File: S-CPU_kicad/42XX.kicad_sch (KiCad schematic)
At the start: 161 parts, among them U34 OR_2, U35 OR_2, U36 OR_2, U37 OR_2, U6 MUX

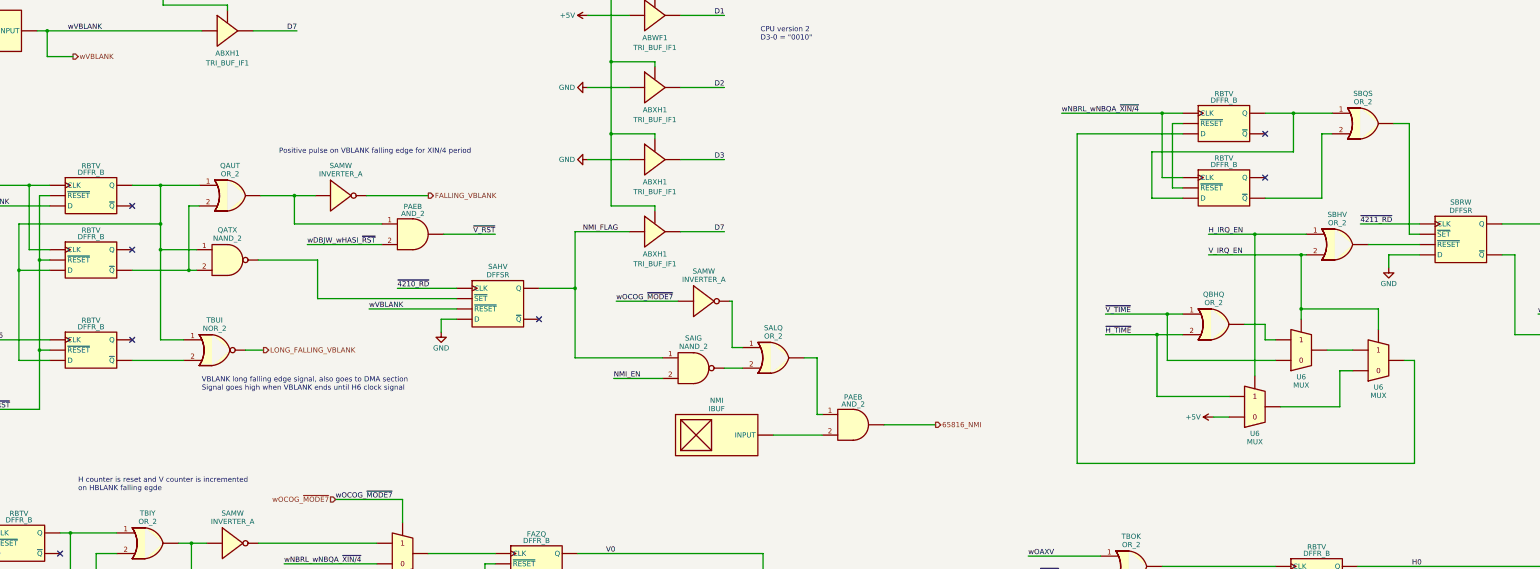
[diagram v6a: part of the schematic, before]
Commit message: DMA section update. Found errors between some MUX and MUXI gates.
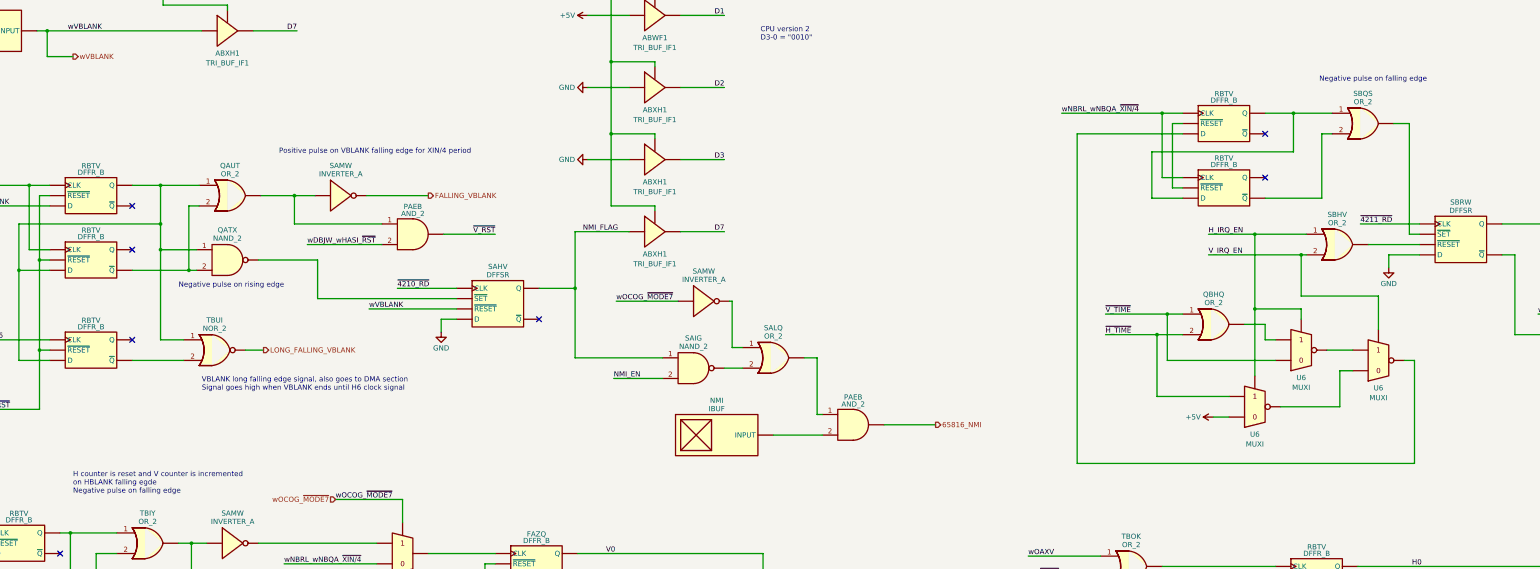
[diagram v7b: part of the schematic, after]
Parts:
- U6: value MUX -> MUXI; symbol Ricoh_Cells:MUX -> Ricoh_Cells:MUXI
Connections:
- net H_IRQ_EN: now also U6.1
- net V_IRQ_EN: no longer U6.1
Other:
- note added: "H counter is reset and V counter is incremented on HBLANK falling egde Negative pulse on falling edge"
- note added: "Negative pulse on falling edge"
- note added: "Negative pulse on rising edge"
- note removed: "H counter is reset and V counter is incremented on HBLANK falling egde"
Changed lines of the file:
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@@
   (junction (at 120.015 297.18) (diameter 0) (color 0 0 0 0)
   )
+  (junction (at 602.615 163.83) (diameter 0) (color 0 0 0 0)
+  )
   (junction (at 173.355 403.86) (diameter 0) (color 0 0 0 0)
   )
@@
   (junction (at 122.555 377.19) (diameter 0) (color 0 0 0 0)
   )
-  (junction (at 614.045 163.83) (diameter 0) (color 0 0 0 0)
-  )
   (junction (at 173.355 288.29) (diameter 0) (color 0 0 0 0)
   )
@@
     (stroke (width 0) (type default))
   )
-  (wire (pts (xy 633.095 163.83) (xy 614.045 163.83))
+  (wire (pts (xy 633.095 160.655) (xy 614.045 160.655))
     (stroke (width 0) (type default))
   )
@@
     (stroke (width 0) (type default))
   )
-  (wire (pts (xy 633.095 168.91) (xy 633.095 163.83))
+  (wire (pts (xy 633.095 168.91) (xy 633.095 160.655))
     (stroke (width 0) (type default))
   )
@@
     (stroke (width 0) (type default))
   )
-  (wire (pts (xy 614.045 150.495) (xy 614.045 163.83))
+  (wire (pts (xy 614.045 150.495) (xy 614.045 160.655))
     (stroke (width 0) (type default))
   )
@@
     (stroke (width 0) (type default))
   )
-  (wire (pts (xy 602.615 145.415) (xy 602.615 180.34))
+  (wire (pts (xy 602.615 145.415) (xy 602.615 163.83))
     (stroke (width 0) (type default))
   )
@@
     (stroke (width 0) (type default))
   )
+  (wire (pts (xy 602.615 163.83) (xy 602.615 180.34))
+    (stroke (width 0) (type default))
+  )
   (wire (pts (xy 132.715 236.22) (xy 147.32 236.22))
     (stroke (width 0) (type default))
@@
     (stroke (width 0) (type dash))
   )
+  (wire (pts (xy 614.045 163.83) (xy 602.615 163.83))
+    (stroke (width 0) (type default))
+  )
   (wire (pts (xy 147.32 283.21) (xy 127.635 283.21))
     (stroke (width 0) (type default))
@@
     (stroke (width 0) (type default))
   )
+  (wire (pts (xy 614.045 166.37) (xy 614.045 163.83))
+    (stroke (width 0) (type default))
+  )
   (wire (pts (xy 341.63 149.225) (xy 332.74 149.225))
     (stroke (width 0) (type default))
@@
     (stroke (width 0) (type default))
   )
-  (wire (pts (xy 614.045 163.83) (xy 614.045 166.37))
-    (stroke (width 0) (type default))
-  )
   (wire (pts (xy 147.32 346.71) (xy 120.015 346.71))
     (stroke (width 0) (type default))
@@
     (effects (font (size 5 5) (thickness 1) bold) (justify left bottom))
   )
+  (text "Negative pulse on rising edge" (at 337.185 158.75 0)
+    (effects (font (size 1.27 1.27)) (justify left bottom))
+  )
   (text "Positive pulse on VBLANK falling edge for XIN/4 period"
     (at 361.95 125.73 0)
@@
     (effects (font (size 2 2)) (justify left bottom))
   )
-  (text "H counter is reset and V counter is incremented\non HBLANK falling egde"
-    (at 312.42 208.915 0)
+  (text "H counter is reset and V counter is incremented\non HBLANK falling egde\nNegative pulse on falling edge"
+    (at 311.15 209.55 0)
     (effects (font (size 1.27 1.27)) (justify left bottom))
   )
@@
     (effects (font (size 5 5) (thickness 1) bold) (justify left bottom))
   )
+  (text "Negative pulse on falling edge" (at 618.49 107.95 0)
+    (effects (font (size 1.27 1.27)) (justify left bottom))
+  )
   (text "4210 READ" (at 439.42 63.5 0)
     (effects (font (size 5 5) (thickness 1) bold) (justify left bottom))
@@
     )
   )
-  (symbol (lib_id "Ricoh_Cells:MUX") (at 614.045 173.99 0) (unit 1)
+  (symbol (lib_id "Ricoh_Cells:MUXI") (at 614.045 173.99 0) (unit 1)
     (in_bom yes) (on_board yes) (dnp no) (fields_autoplaced)
-    (property "Reference" "U6" (at 614.045 180.602 0)
+    (property "Reference" "U6" (at 614.045 180.7901 0)
       (effects (font (size 1.27 1.27)))
     )
-    (property "Value" "MUX" (at 614.045 182.65 0)
+    (property "Value" "MUXI" (at 614.045 183.2143 0)
       (effects (font (size 1.27 1.27)))
     )
@@
       (effects (font (size 1.27 1.27)) hide)
     )
-    (property "Datasheet" "http://iceboy.a-singer.de/doc/dmg_cells.html#mux" (at 614.045 186.055 0)
+    (property "Datasheet" "http://iceboy.a-singer.de/doc/dmg_cells.html#muxi" (at 614.045 186.055 0)
       (effects (font (size 1.27 1.27)) hide)
     )
@@
         )
         (path "/ca9d3ca9-0297-4b98-a109-b7c162ccc5c3/4dc5cd9a-499d-4e55-930f-d6021c4e63f2"
-          (reference "SBFO0") (unit 1)
+          (reference "SBFO1") (unit 1)
         )
       )
@@
     )
   )
-  (symbol (lib_id "Ricoh_Cells:MUX") (at 633.095 176.53 0) (unit 1)
+  (symbol (lib_id "Ricoh_Cells:MUXI") (at 633.095 176.53 0) (unit 1)
     (in_bom yes) (on_board yes) (dnp no) (fields_autoplaced)
-    (property "Reference" "U6" (at 633.095 183.142 0)
+    (property "Reference" "U6" (at 633.095 183.3301 0)
       (effects (font (size 1.27 1.27)))
     )
-    (property "Value" "MUX" (at 633.095 185.19 0)
+    (property "Value" "MUXI" (at 633.095 185.7543 0)
       (effects (font (size 1.27 1.27)))
     )
@@
       (effects (font (size 1.27 1.27)) hide)
     )
-    (property "Datasheet" "http://iceboy.a-singer.de/doc/dmg_cells.html#mux" (at 633.095 188.595 0)
+    (property "Datasheet" "http://iceboy.a-singer.de/doc/dmg_cells.html#muxi" (at 633.095 188.595 0)
       (effects (font (size 1.27 1.27)) hide)
     )
@@
         )
         (path "/ca9d3ca9-0297-4b98-a109-b7c162ccc5c3/4dc5cd9a-499d-4e55-930f-d6021c4e63f2"
-          (reference "SBFO2") (unit 1)
+          (reference "SBFU") (unit 1)
         )
       )
@@
     )
   )
-  (symbol (lib_id "Ricoh_Cells:MUX") (at 602.615 187.96 0) (unit 1)
+  (symbol (lib_id "Ricoh_Cells:MUXI") (at 602.615 187.96 0) (unit 1)
     (in_bom yes) (on_board yes) (dnp no) (fields_autoplaced)
-    (property "Reference" "U6" (at 602.615 194.572 0)
+    (property "Reference" "U6" (at 602.615 194.7601 0)
       (effects (font (size 1.27 1.27)))
     )
-    (property "Value" "MUX" (at 602.615 196.62 0)
+    (property "Value" "MUXI" (at 602.615 197.1843 0)
       (effects (font (size 1.27 1.27)))
     )
@@
       (effects (font (size 1.27 1.27)) hide)
     )
-    (property "Datasheet" "http://iceboy.a-singer.de/doc/dmg_cells.html#mux" (at 602.615 200.025 0)
+    (property "Datasheet" "http://iceboy.a-singer.de/doc/dmg_cells.html#muxi" (at 602.615 200.025 0)
       (effects (font (size 1.27 1.27)) hide)
     )
@@
         )
         (path "/ca9d3ca9-0297-4b98-a109-b7c162ccc5c3/4dc5cd9a-499d-4e55-930f-d6021c4e63f2"
-          (reference "SBFO1") (unit 1)
+          (reference "SBFO0") (unit 1)
         )
       )
